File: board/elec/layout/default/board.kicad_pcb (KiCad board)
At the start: 2 copper layers, 165 x 67 mm, 5 parts

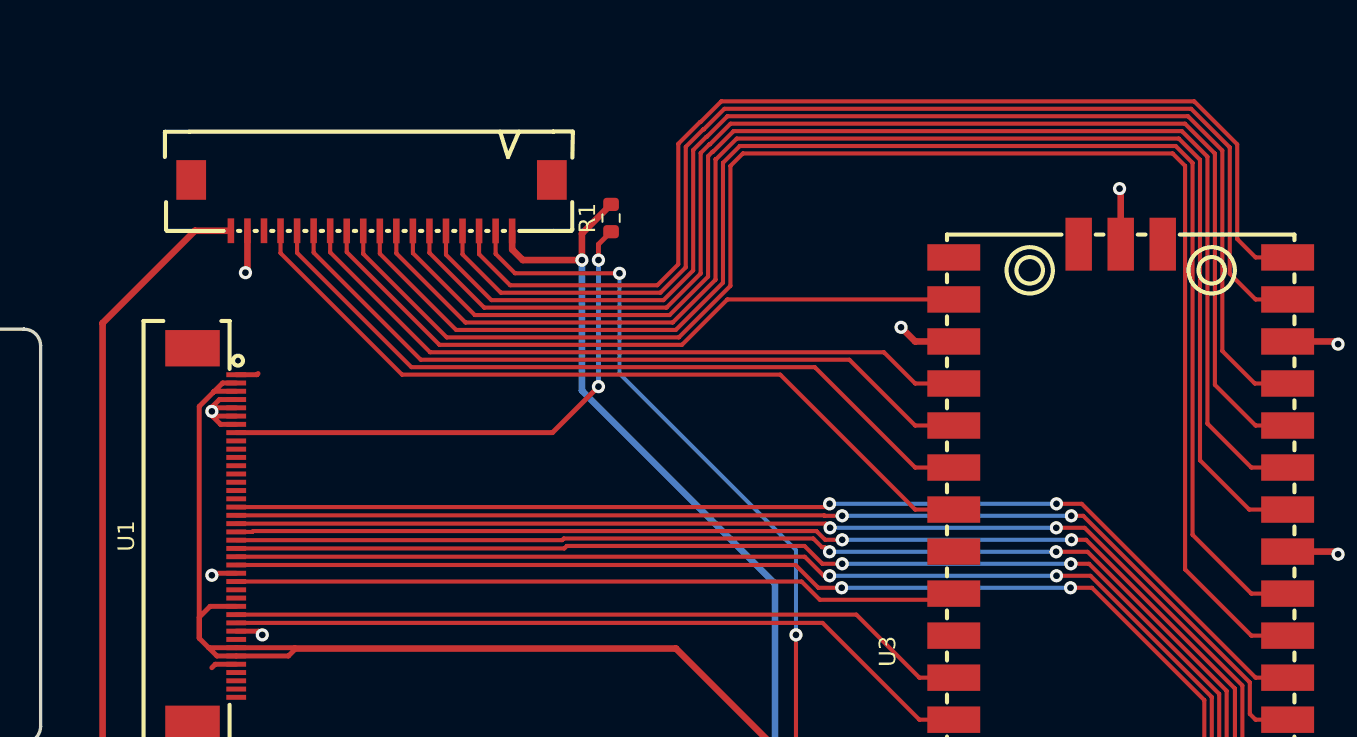
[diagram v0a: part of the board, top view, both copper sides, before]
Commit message: correct 3d model settings.
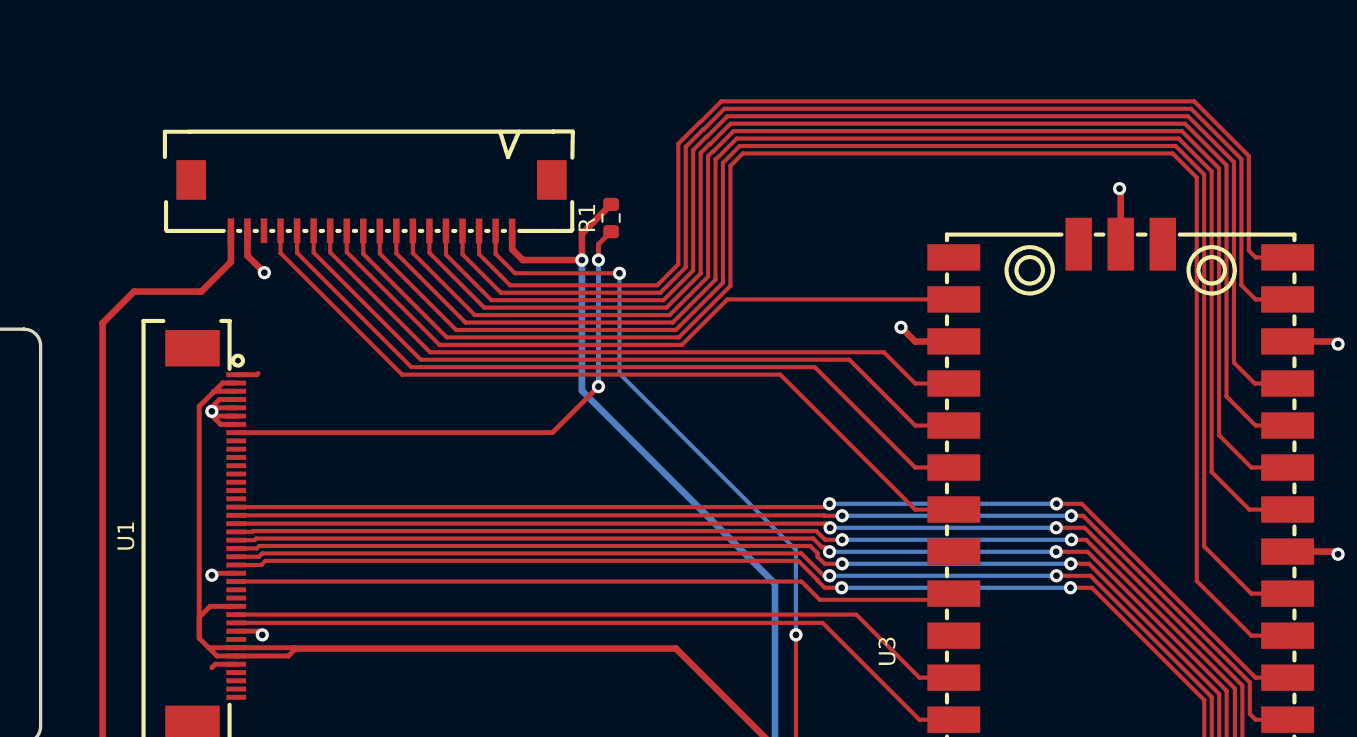
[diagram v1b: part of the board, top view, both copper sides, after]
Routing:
- net vdd5: track 94.3 -> 95.4 mm
